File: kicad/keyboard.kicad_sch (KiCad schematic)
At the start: 119 parts, among them SW1 SW_MX, SW10 SW_MX, SW11 SW_MX, SW12 SW_MX, SW13 SW_MX, SW14 SW_MX, SW15 SW_MX, SW16 SW_MX, SW17 SW_MX, SW18 SW_MX, SW19 SW_MX, SW2 SW_MX, SW20 SW_MX, SW21 SW_MX, SW22 SW_MX, SW23 SW_MX, SW24 SW_MX, SW25 SW_MX, SW26 SW_MX, SW27 SW_MX, SW28 SW_MX, SW29 SW_MX, SW3 SW_MX, SW30 SW_MX, SW31 SW_MX, SW32 SW_MX, SW33 SW_MX, SW34 SW_MX, SW35 SW_MX, SW36 SW_MX, SW37 SW_MX, SW38 SW_MX, SW39 SW_MX, SW4 SW_MX, SW40 SW_MX, SW41 SW_MX, SW42 SW_MX, SW43 SW_MX, SW44 SW_MX, SW45 SW_MX, SW46 SW_MX, SW47 SW_MX, SW48 SW_MX, SW49 SW_MX, SW5 SW_MX, SW50 SW_MX, SW51 SW_MX, SW52 SW_MX, SW53 SW_MX, SW54 SW_MX, SW55 SW_MX, SW56 SW_MX, SW57 SW_MX, SW58 SW_MX, SW59 SW_MX, SW6 SW_MX, SW7 SW_MX, SW8 SW_MX, SW9 SW_MX

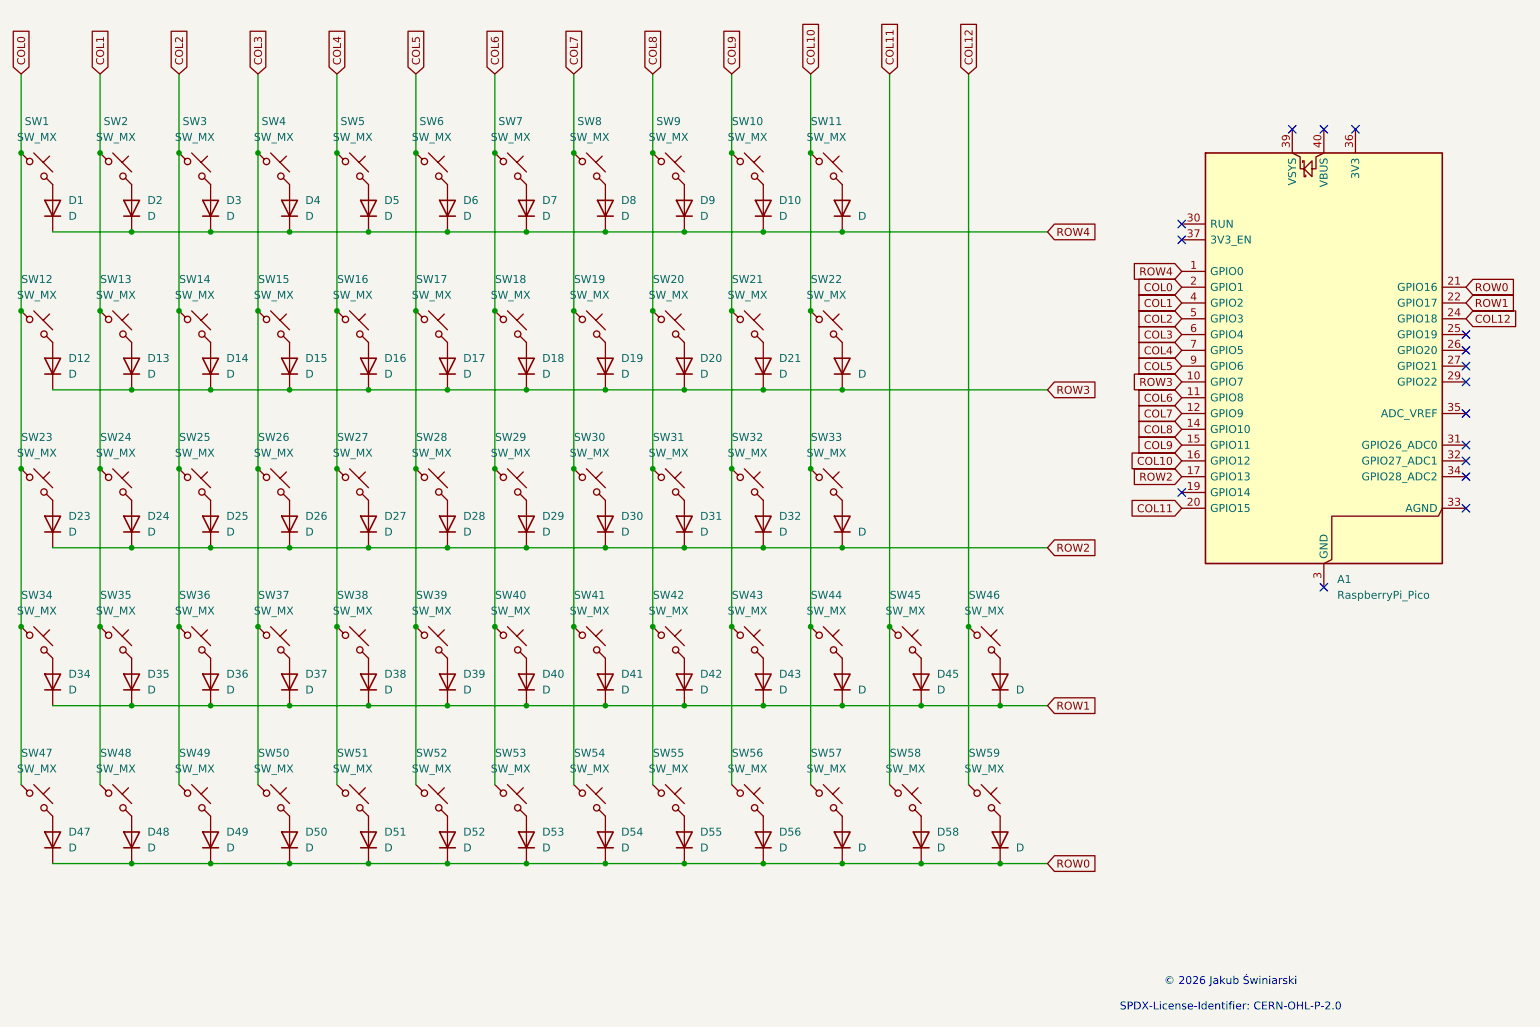
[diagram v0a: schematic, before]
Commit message: Update schematic and redesign PCB
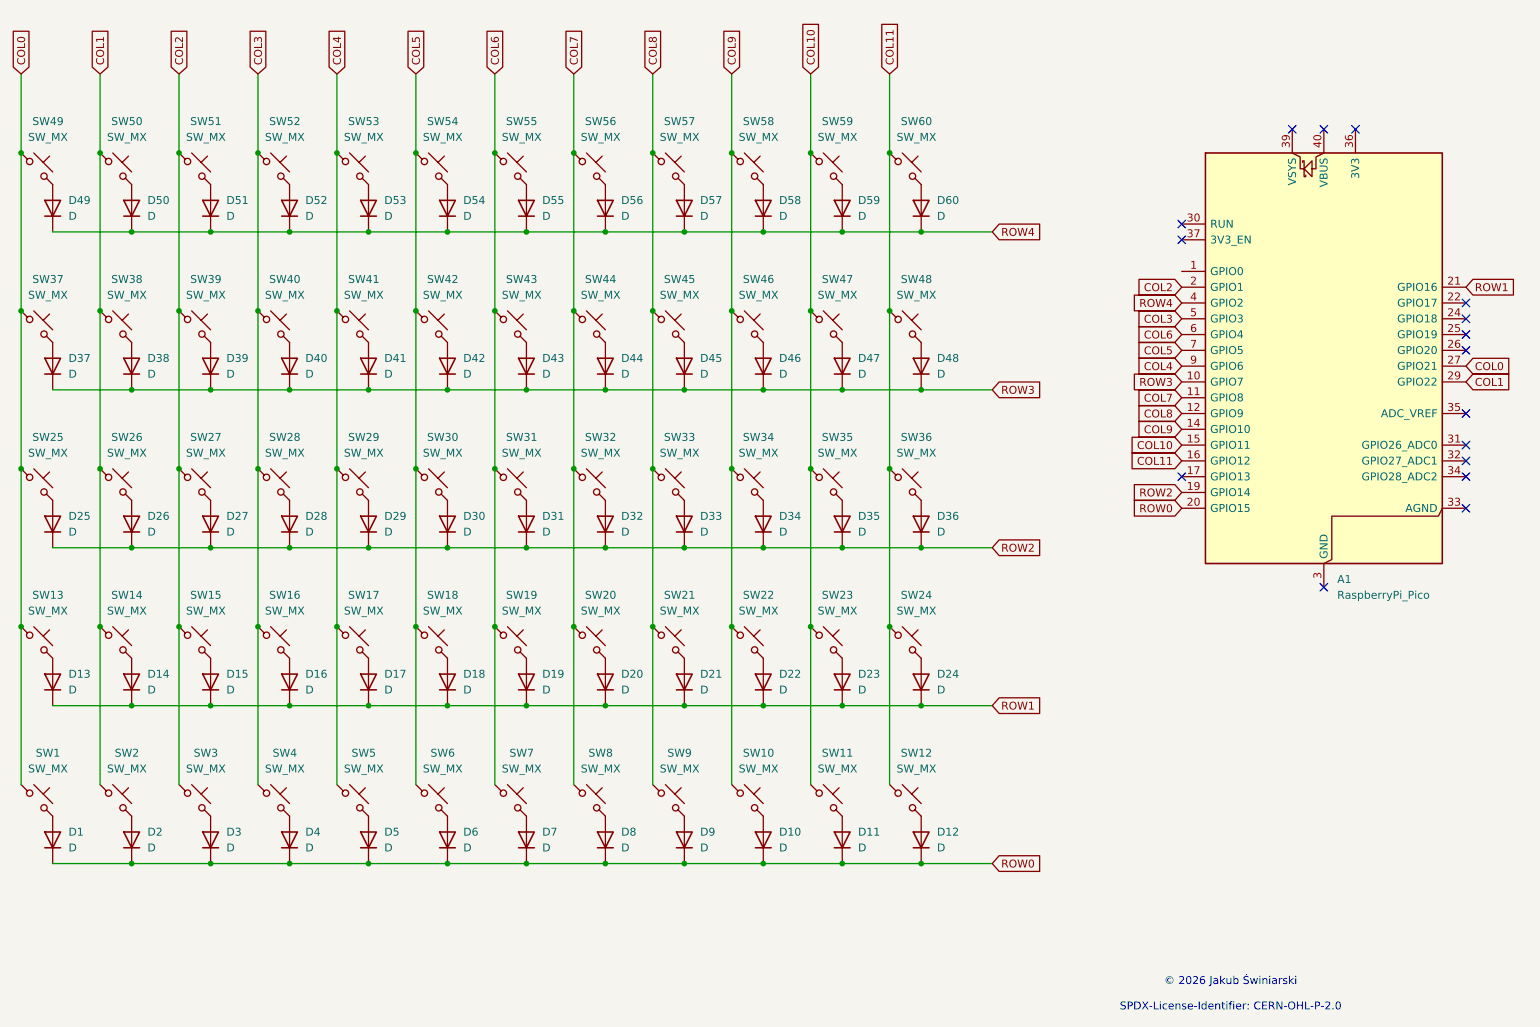
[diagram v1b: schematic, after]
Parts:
- added D60: D, Diode_THT:D_DO-35_SOD27_P7.62mm_Horizontal, symbol Device:D
- added SW60: SW_MX, Button_Switch_Keyboard:SW_Cherry_MX_1.00u_PCB, symbol Switch:SW_Push_45deg
- renumbered D47 to D1, D56 to D10, D57 to D11, D58 to D12, D34 to D13, D35 to D14, D36 to D15, D37 to D16, D38 to D17, D39 to D18, D40 to D19, D48 to D2, D41 to D20, D42 to D21, D43 to D22, D44 to D23, D45 to D24, D23 to D25, D24 to D26, D25 to D27, D26 to D28, D27 to D29, D49 to D3, D28 to D30, D29 to D31, D30 to D32, D31 to D33, D32 to D34, D33 to D35, D46 to D36, D12 to D37, D13 to D38, D14 to D39, D50 to D4, D15 to D40, D16 to D41, D17 to D42, D18 to D43, D19 to D44, D20 to D45, D21 to D46, D22 to D47, D59 to D48, D1 to D49, D51 to D5, D2 to D50, D3 to D51, D4 to D52, D5 to D53, D6 to D54, D7 to D55, D8 to D56, D9 to D57, D10 to D58, D11 to D59, D52 to D6, D53 to D7, D54 to D8, D55 to D9, SW47 to SW1, SW56 to SW10, SW57 to SW11, SW58 to SW12, SW34 to SW13, SW35 to SW14, SW36 to SW15, SW37 to SW16, SW38 to SW17, SW39 to SW18, SW40 to SW19, SW48 to SW2, SW41 to SW20, SW42 to SW21, SW43 to SW22, SW44 to SW23, SW45 to SW24, SW23 to SW25, SW24 to SW26, SW25 to SW27, SW26 to SW28, SW27 to SW29, SW49 to SW3, SW28 to SW30, SW29 to SW31, SW30 to SW32, SW31 to SW33, SW32 to SW34, SW33 to SW35, SW46 to SW36, SW12 to SW37, SW13 to SW38, SW14 to SW39, SW50 to SW4, SW15 to SW40, SW16 to SW41, SW17 to SW42, SW18 to SW43, SW19 to SW44, SW20 to SW45, SW21 to SW46, SW22 to SW47, SW59 to SW48, SW1 to SW49, SW51 to SW5, SW2 to SW50, SW3 to SW51, SW4 to SW52, SW5 to SW53, SW6 to SW54, SW7 to SW55, SW8 to SW56, SW9 to SW57, SW10 to SW58, SW11 to SW59, SW52 to SW6, SW53 to SW7, SW54 to SW8, SW55 to SW9
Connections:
- net COL0: now also A1.27 (GPIO21); no longer A1.2 (GPIO1)
- net COL1: now also A1.29 (GPIO22); no longer A1.4 (GPIO2)
- net COL10: now also A1.15 (GPIO11); no longer A1.16 (GPIO12)
- net COL11: now also A1.16 (GPIO12), SW36.1, SW48.1, SW60.1; no longer A1.20 (GPIO15)
- net COL2: now also A1.2 (GPIO1); no longer A1.5 (GPIO3)
- net COL3: now also A1.5 (GPIO3); no longer A1.6 (GPIO4)
- net COL4: now also A1.9 (GPIO6); no longer A1.7 (GPIO5)
- net COL5: now also A1.7 (GPIO5); no longer A1.9 (GPIO6)
- net COL6: now also A1.6 (GPIO4); no longer A1.11 (GPIO8)
- net COL7: now also A1.11 (GPIO8); no longer A1.12 (GPIO9)
- net COL8: now also A1.12 (GPIO9); no longer A1.14 (GPIO10)
- net COL9: now also A1.14 (GPIO10); no longer A1.15 (GPIO11)
- net ROW0: now also A1.20 (GPIO15); no longer A1.21 (GPIO16), D48.1 (K)
- net ROW1: now also A1.21 (GPIO16); no longer A1.22 (GPIO17), D36.1 (K)
- net ROW2: now also A1.19 (GPIO14), D36.1 (K); no longer A1.17 (GPIO13)
- net ROW3: now also D48.1 (K)
- net ROW4: now also A1.4 (GPIO2), D60.1 (K); no longer A1.1 (GPIO0)
- removed net COL12: A1.24 (GPIO18), SW36.1, SW48.1
- new net: D60.2 (A), SW60.2
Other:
- moved on the sheet: SW36, SW48
